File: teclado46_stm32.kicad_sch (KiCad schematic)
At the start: 12 parts, among them J2 78171-0004, U1 XC6206PxxxMR, U2 STM32G474CETx, U4 W25Q128JVS

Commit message: chore: routed rows
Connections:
- net ROW 0: now also U2.43 (PB6)
- net ROW 1: now also U2.42 (PB5)
- net ROW 2: now also U2.37 (PA13)
- net ROW 3: now also U2.18 (PB2)
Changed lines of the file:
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@@
 	(global_label "ROW 1"
 		(shape input)
-		(at 119.38 113.03 180)
-		(fields_autoplaced yes)
-		(effects
-			(font
-				(size 1.27 1.27)
-			)
-			(justify right)
-		)
-		(property "Intersheetrefs" "${INTERSHEET_REFS}"
-			(at 110.1658 113.03 0)
+		(at 33.02 151.13 180)
+		(fields_autoplaced yes)
+		(effects
+			(font
+				(size 1.27 1.27)
+			)
+			(justify right)
+		)
+		(property "Intersheetrefs" "${INTERSHEET_REFS}"
+			(at 23.8058 151.13 0)
 			(effects
 				(font
@@
 	(global_label "ROW 0"
 		(shape input)
-		(at 119.38 110.49 180)
-		(fields_autoplaced yes)
-		(effects
-			(font
-				(size 1.27 1.27)
-			)
-			(justify right)
-		)
-		(property "Intersheetrefs" "${INTERSHEET_REFS}"
-			(at 110.1658 110.49 0)
+		(at 33.02 153.67 180)
+		(fields_autoplaced yes)
+		(effects
+			(font
+				(size 1.27 1.27)
+			)
+			(justify right)
+		)
+		(property "Intersheetrefs" "${INTERSHEET_REFS}"
+			(at 23.8058 153.67 0)
 			(effects
 				(font
@@
 	(global_label "ROW 2"
 		(shape input)
-		(at 114.3 119.38 0)
-		(fields_autoplaced yes)
-		(effects
-			(font
-				(size 1.27 1.27)
-			)
-			(justify left)
-		)
-		(property "Intersheetrefs" "${INTERSHEET_REFS}"
-			(at 123.5142 119.38 0)
+		(at 68.58 143.51 0)
+		(fields_autoplaced yes)
+		(effects
+			(font
+				(size 1.27 1.27)
+			)
+			(justify left)
+		)
+		(property "Intersheetrefs" "${INTERSHEET_REFS}"
+			(at 77.7942 143.51 0)
 			(effects
 				(font
@@
 	(global_label "ROW 3"
 		(shape input)
-		(at 114.3 121.92 0)
-		(fields_autoplaced yes)
-		(effects
-			(font
-				(size 1.27 1.27)
-			)
-			(justify left)
-		)
-		(property "Intersheetrefs" "${INTERSHEET_REFS}"
-			(at 123.5142 121.92 0)
-			(effects
-				(font
-					(size 1.27 1.27)
-				)
-				(justify left)
-				(hide yes)
-			)
+		(at 33.02 143.51 180)
+		(fields_autoplaced yes)
+		(effects
+			(font
+				(size 1.27 1.27)
+			)
+			(justify right)
+		)
+		(property "Intersheetrefs" "${INTERSHEET_REFS}"
+			(at 23.8058 143.51 0)
+			(effects
+				(font
+					(size 1.27 1.27)
+				)
+				(justify right)
+				(hide yes)
+			)

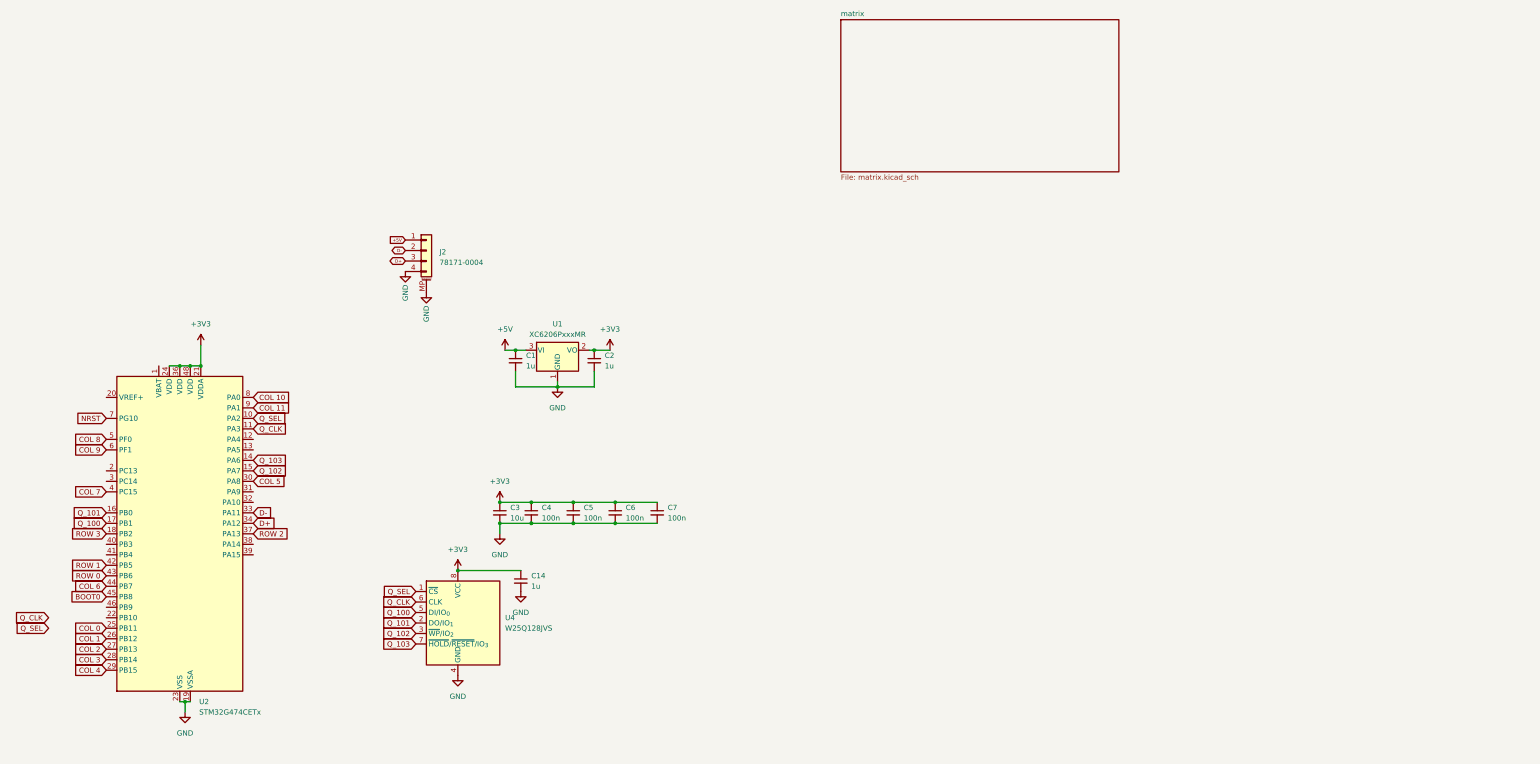
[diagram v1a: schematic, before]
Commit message: chore: change to g0b1ret6
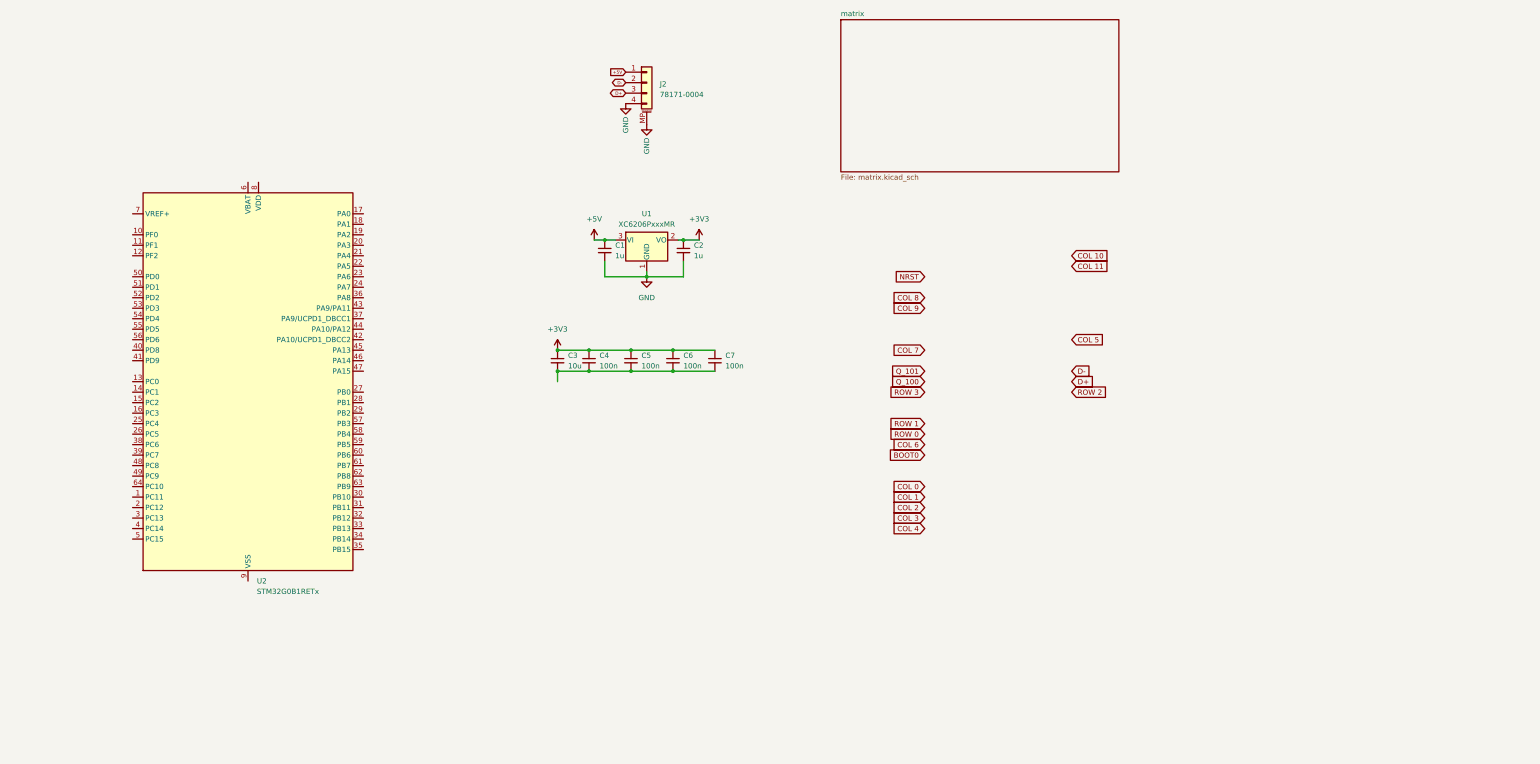
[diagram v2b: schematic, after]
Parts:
- removed C14: 1u, Capacitor_SMD:C_0402_1005Metric, symbol Device:C_Small
- removed U2: STM32G474CETx, Package_QFP:LQFP-48_7x7mm_P0.5mm, symbol MCU_ST_STM32G4:STM32G474CETx
- removed U4: W25Q128JVS, Package_SO:SOIC-8_5.3x5.3mm_P1.27mm, symbol Memory_Flash:W25Q128JVS
- added U2: STM32G0B1RETx, Package_QFP:LQFP-64_10x10mm_P0.5mm, symbol MCU_ST_STM32G0:STM32G0B1RETx
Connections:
- net GND: no longer C3.2, C4.2, C5.2, C6.2, C7.2
- new net: C3.2, C4.2, C5.2, C6.2, C7.2
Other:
- moved on the sheet: C1, C2, C3, C4, C5, C6, C7, J2, U1

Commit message: chore: add boot0 and nrst
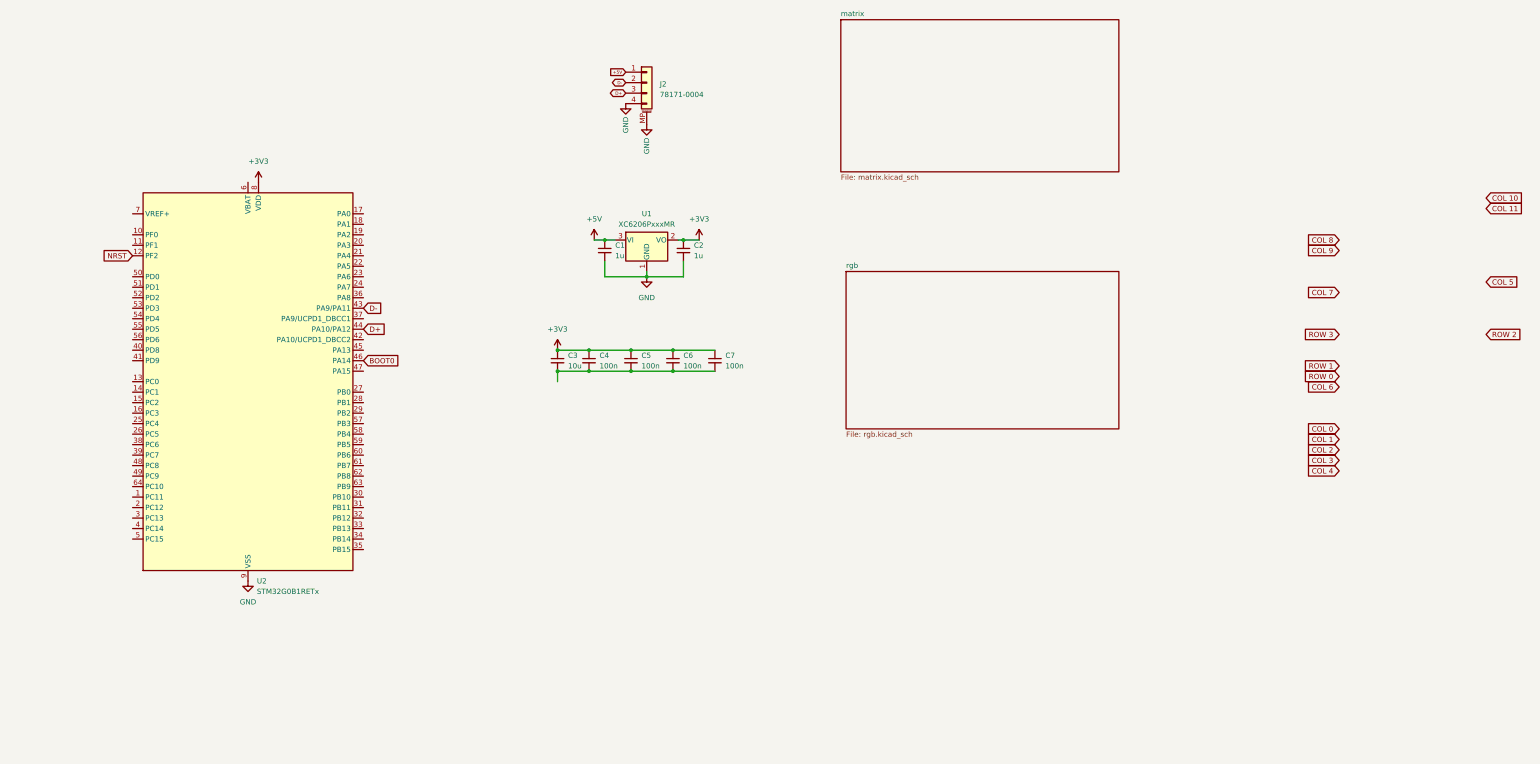
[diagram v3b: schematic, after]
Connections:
- net +3V3: now also U2.8 (VDD)
- net BOOT0: now also U2.46 (PA14)
- net D+: now also U2.44 (PA10/PA12)
- net D-: now also U2.43 (PA9/PA11)
- net GND: now also U2.9 (VSS)
- net NRST: now also U2.12 (PF2)
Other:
- added sheet rgb (rgb.kicad_sch)

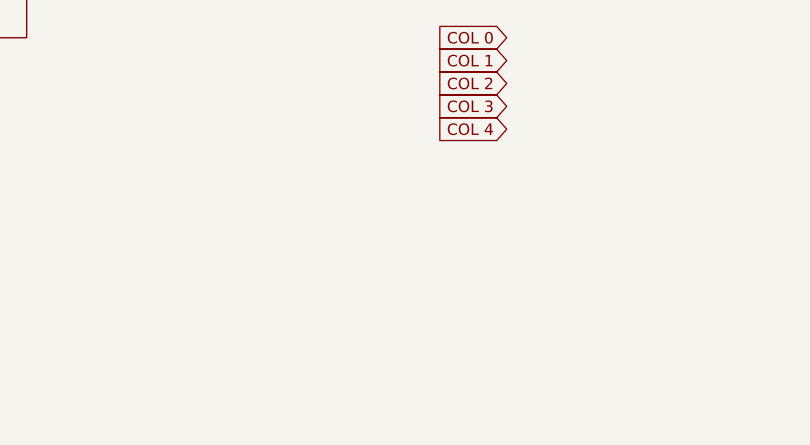
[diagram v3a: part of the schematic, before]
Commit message: chore: add led matrix
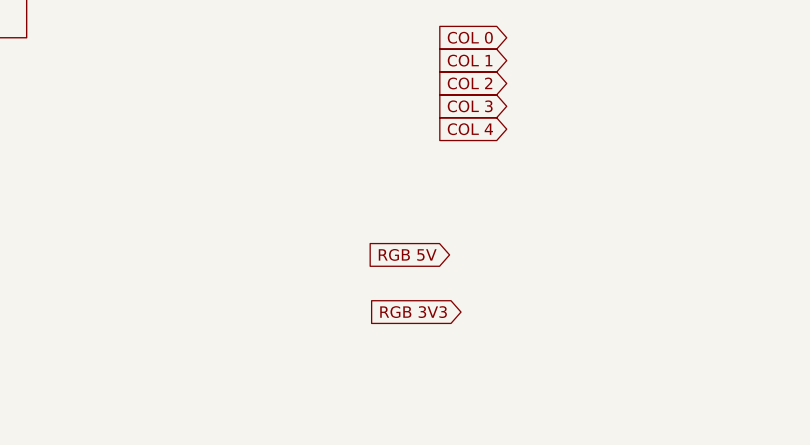
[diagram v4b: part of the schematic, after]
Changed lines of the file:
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@@
+		)
+	)
+	(global_label "RGB 5V"
+		(shape input)
+		(at 325.12 142.24 180)
+		(fields_autoplaced yes)
+		(effects
+			(font
+				(size 1.27 1.27)
+			)
+			(justify right)
+		)
+		(property "Intersheetrefs" "${INTERSHEET_REFS}"
+			(at 315.0591 142.24 0)
+			(effects
+				(font
+					(size 1.27 1.27)
+				)
+				(justify right)
+				(hide yes)
+			)
 		)
 	)
@@
 				)
 				(justify right)
+				(hide yes)
+			)
+		)
+	)
+	(global_label "RGB 3V3"
+		(shape input)
+		(at 326.39 148.59 180)
+		(fields_autoplaced yes)
+		(effects
+			(font
+				(size 1.27 1.27)
+			)
+			(justify right)
+		)
+		(property "Intersheetrefs" "${INTERSHEET_REFS}"
+			(at 315.1196 148.59 0)
+			(effects
+				(font
+					(size 1.27 1.27)
+				)
+				(justify right)

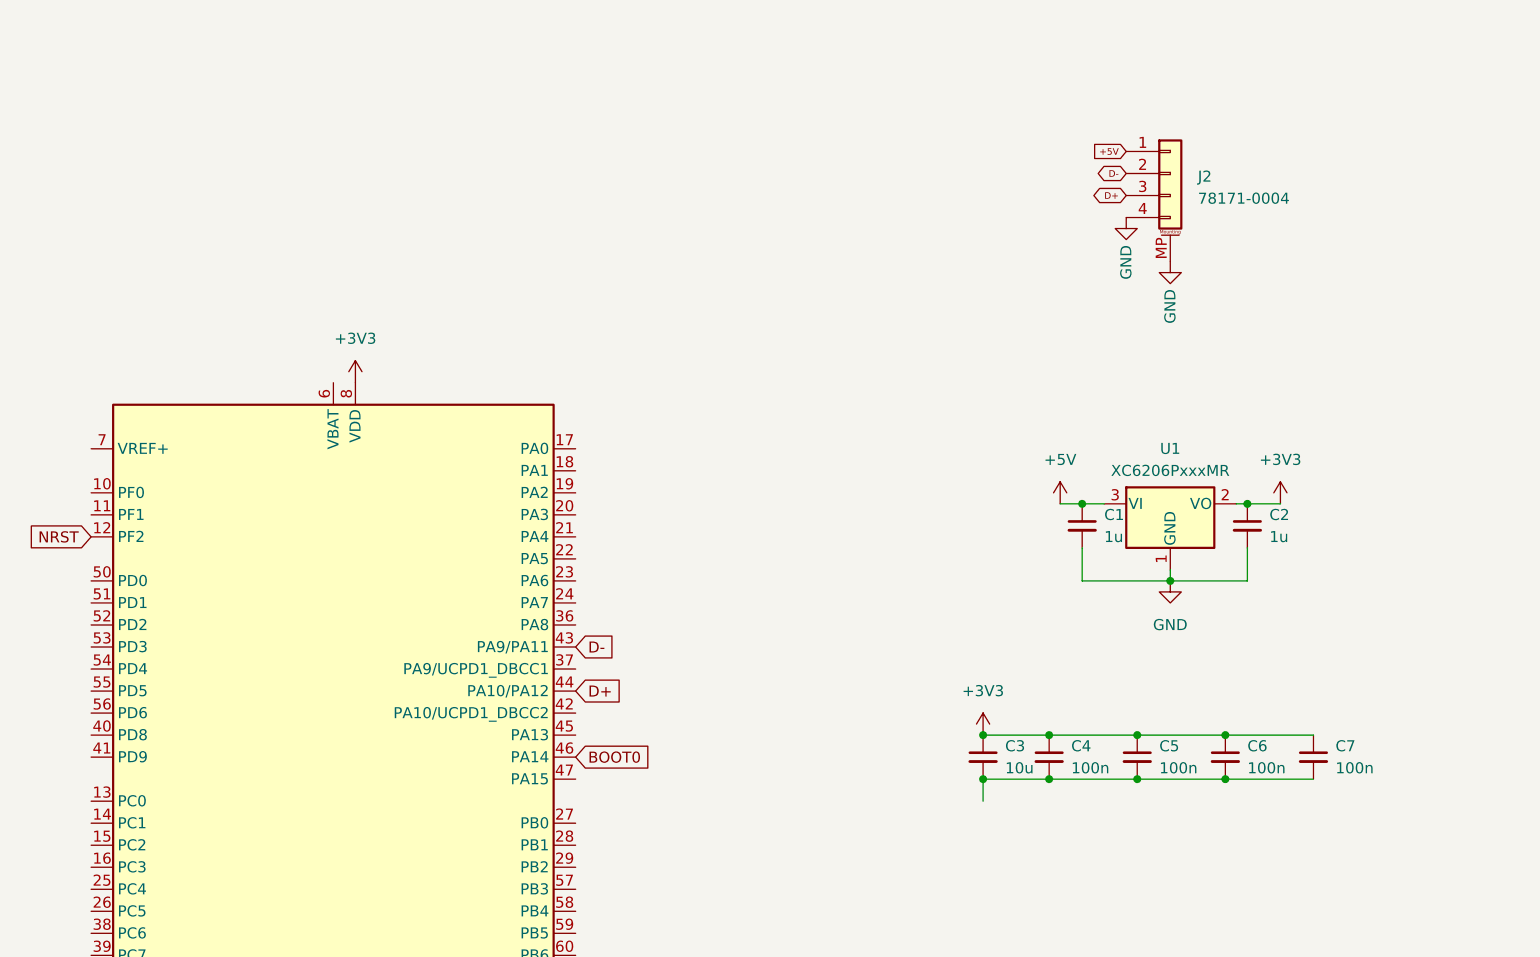
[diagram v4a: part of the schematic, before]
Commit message: chore: routed leds
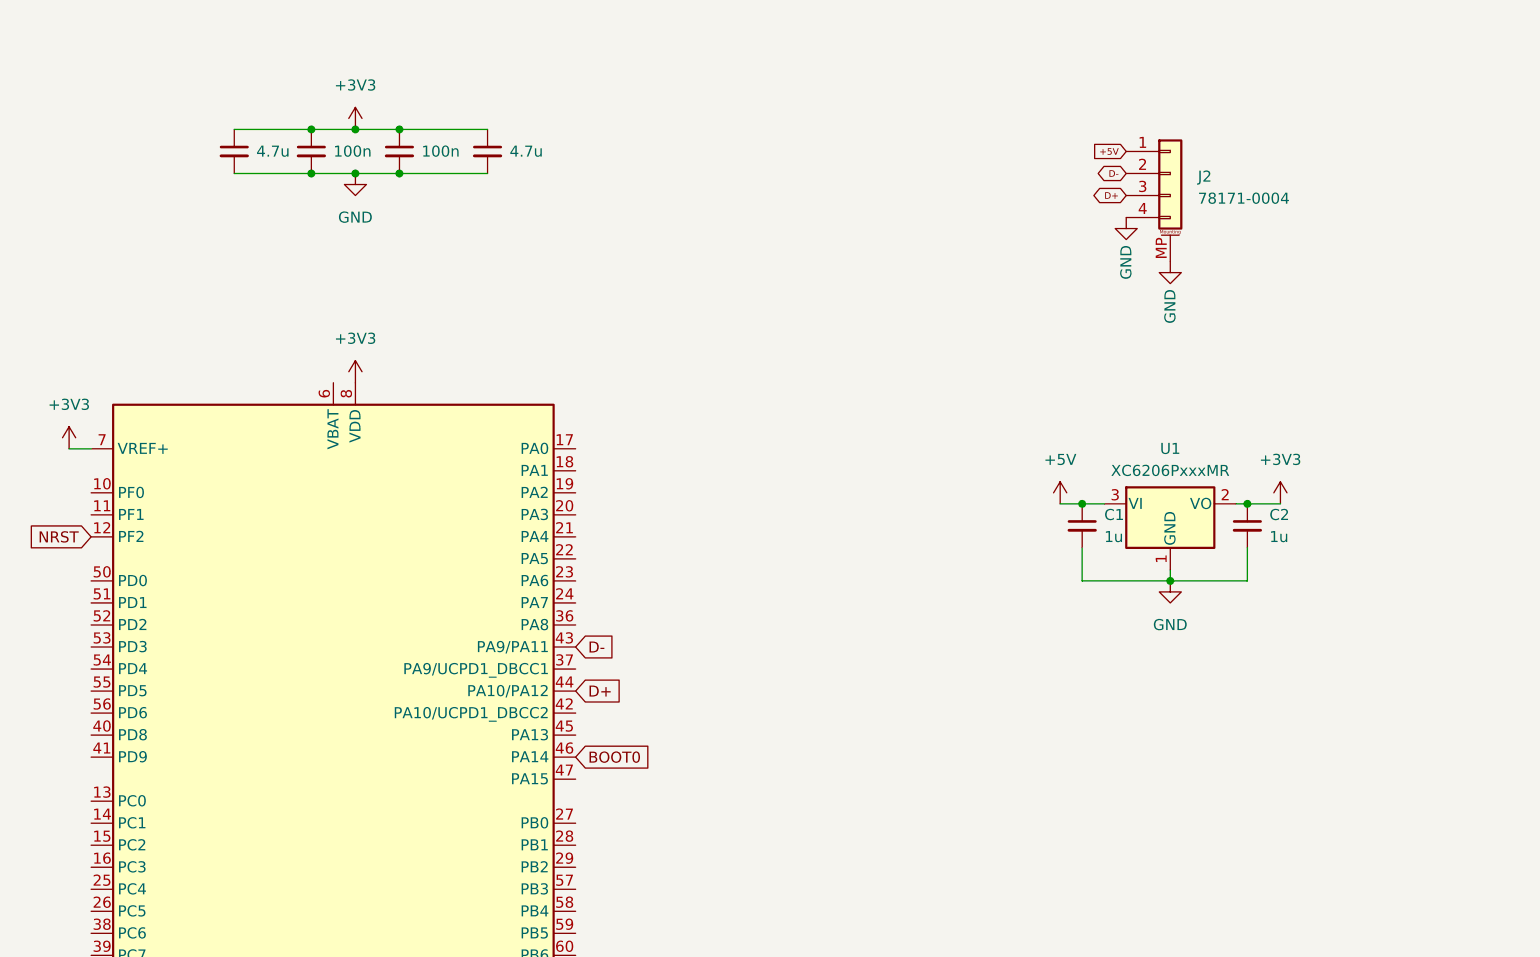
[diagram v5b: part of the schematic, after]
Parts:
- removed C3: 10u, Capacitor_SMD:C_0603_1608Metric, symbol Device:C_Small
- removed C4, C5, C6, C7: 100n, Capacitor_SMD:C_0402_1005Metric, symbol Device:C_Small
- added C14, C16: 100n, Capacitor_SMD:C_0805_2012Metric, symbol Device:C_Small
- added C17, C18: 4.7u, Capacitor_SMD:C_0805_2012Metric, symbol Device:C_Small
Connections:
- net +3V3: now also U2.7 (VREF+), C14.1, C16.1, C17.1, C18.1
- net GND: now also C14.2, C16.2, C17.2, C18.2

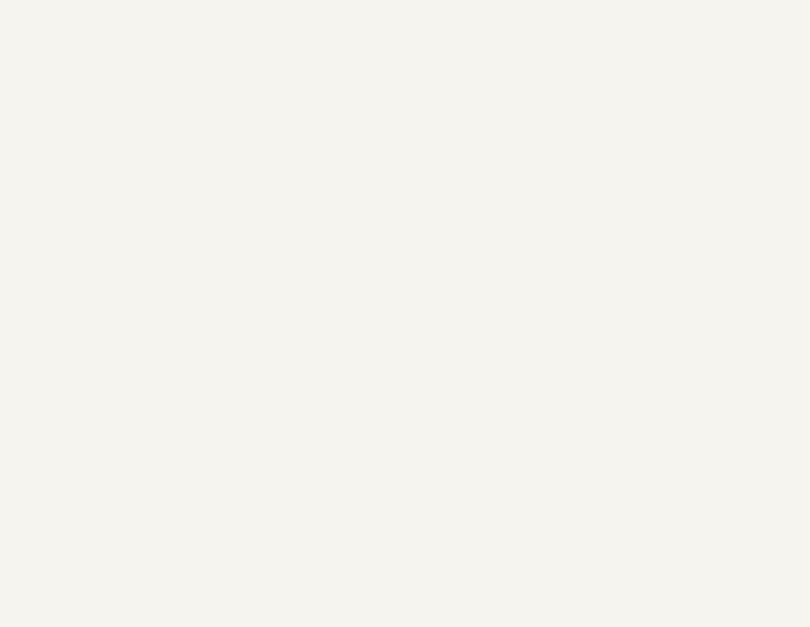
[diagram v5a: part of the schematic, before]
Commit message: chore: routed pre-matrix
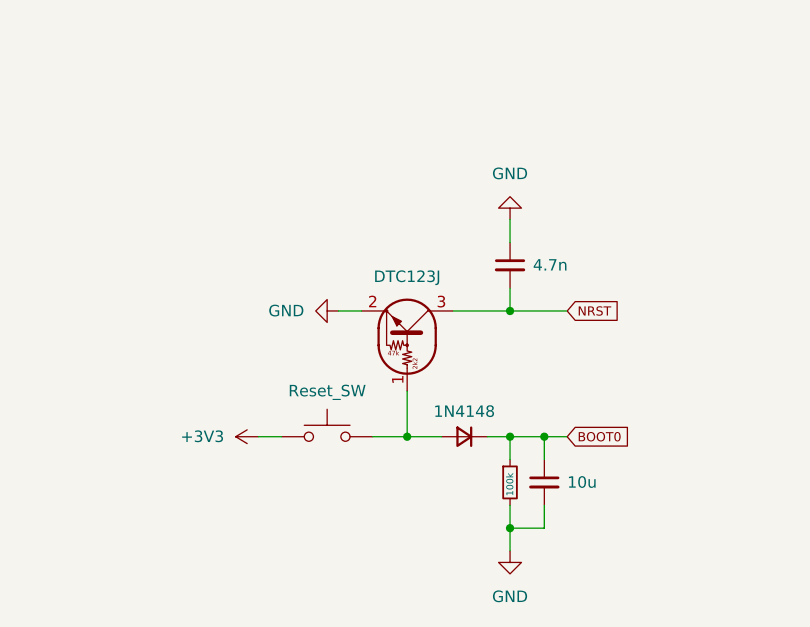
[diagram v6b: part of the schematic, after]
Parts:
- added C12: 4.7n, Capacitor_SMD:C_0805_2012Metric, symbol Device:C_Small
- added C13: 10u, Capacitor_SMD:C_0805_2012Metric, symbol Device:C_Small
- added D47: 1N4148, Diode_SMD:D_SOD-123, symbol Device:D_Small
- added Q1: DTC123J, Package_TO_SOT_SMD:SOT-23, symbol Transistor_BJT:DTC123J
- added R11: 100k, Resistor_SMD:R_0805_2012Metric, symbol Device:R_Small
- added SW1: Reset_SW, PCM_marbastlib-various:SW_SPST_SKQG_WithStem, symbol Switch:SW_Push
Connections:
- net +3V3: now also SW1.1
- net BOOT0: now also C13.1, D47.1 (K), R11.1
- net GND: now also C12.1, C13.2, Q1.2 (E), R11.2
- net NRST: now also C12.2, Q1.3 (C)
- new net: D47.2 (A), Q1.1 (B), SW1.2
